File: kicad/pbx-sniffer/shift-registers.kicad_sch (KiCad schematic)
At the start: 1 part, among them U2 74LS165

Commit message: more shift register work
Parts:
- added J49: Conn_01x02_Socket, Connector_PinSocket_2.54mm:PinSocket_1x02_P2.54mm_Vertical, symbol Connector:Conn_01x02_Socket
- added R1: 10k, symbol Device:R
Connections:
- net +5V: now also J49.2 (Pin_2)
- net GND: now also R1.2
- net at U2.11 (D0): now also J49.1 (Pin_1), R1.1

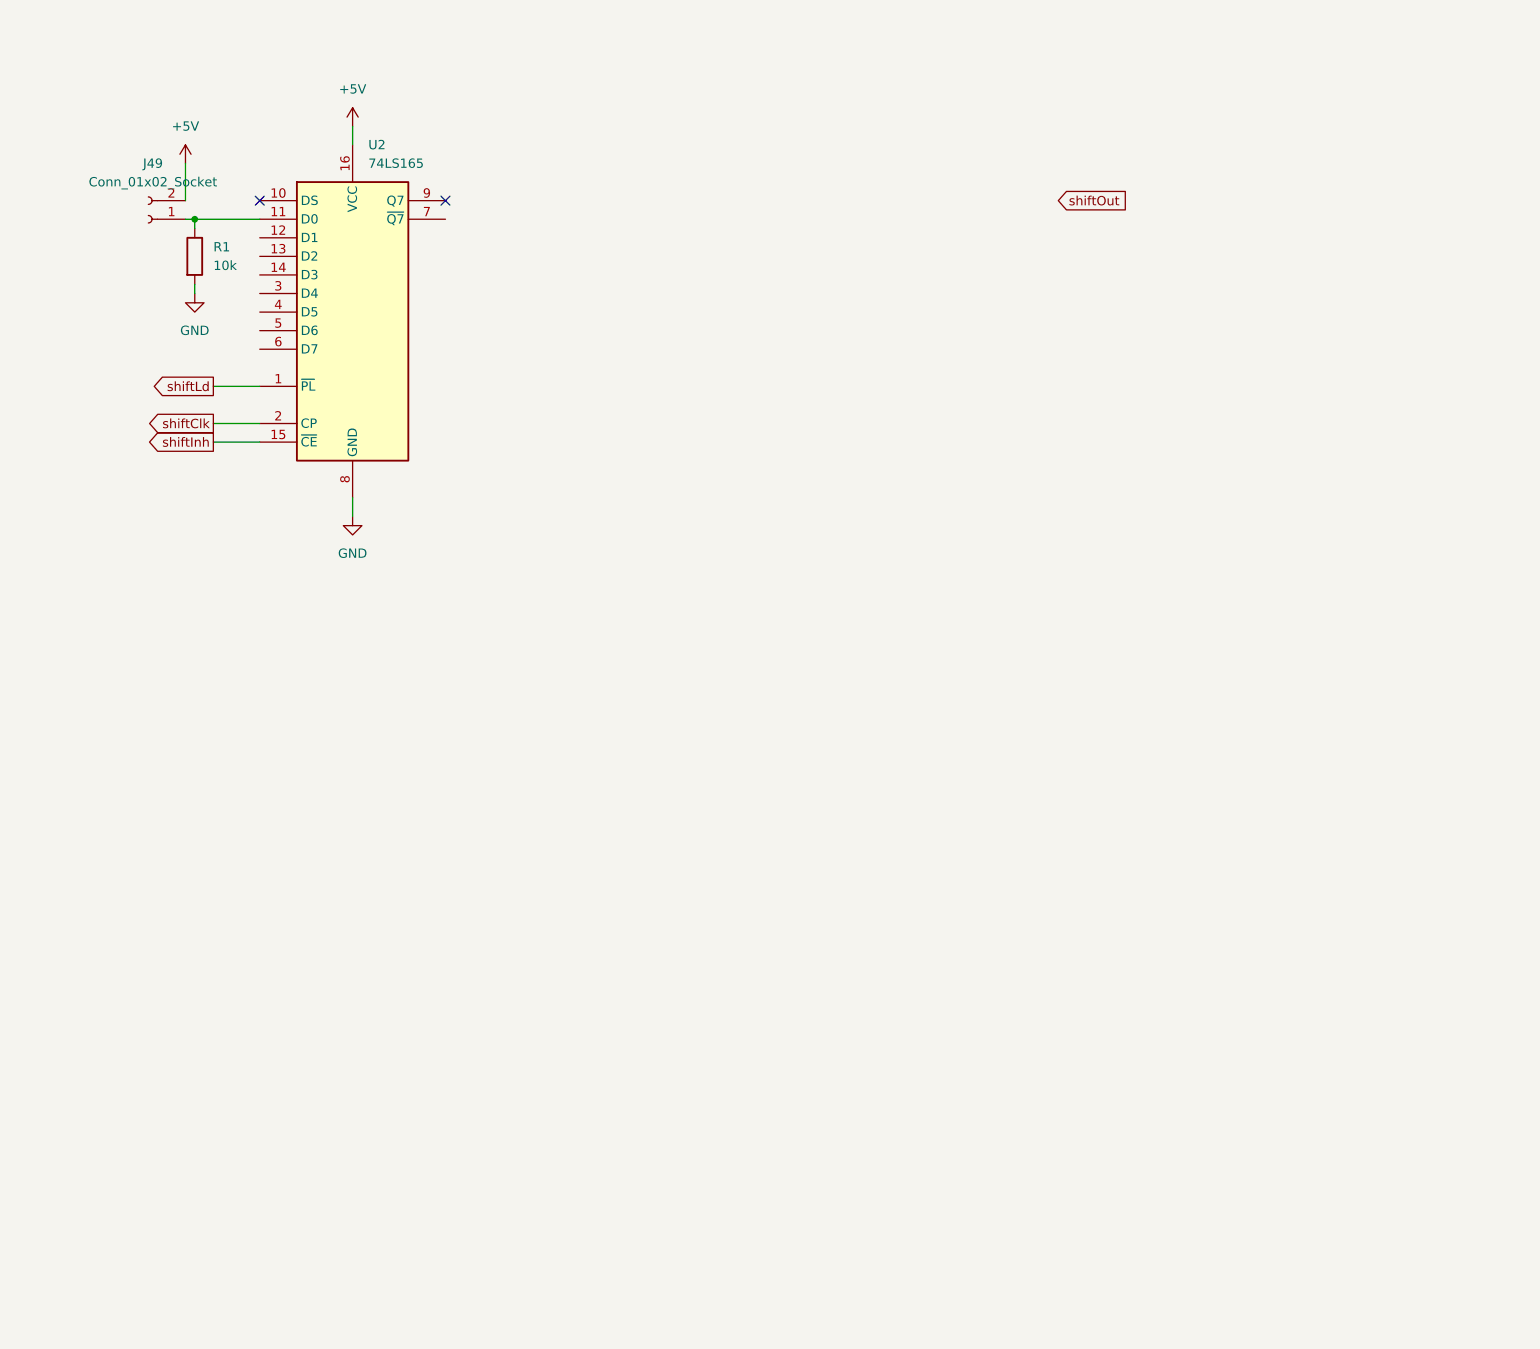
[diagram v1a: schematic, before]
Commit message: shift register page assembled for 16 phones
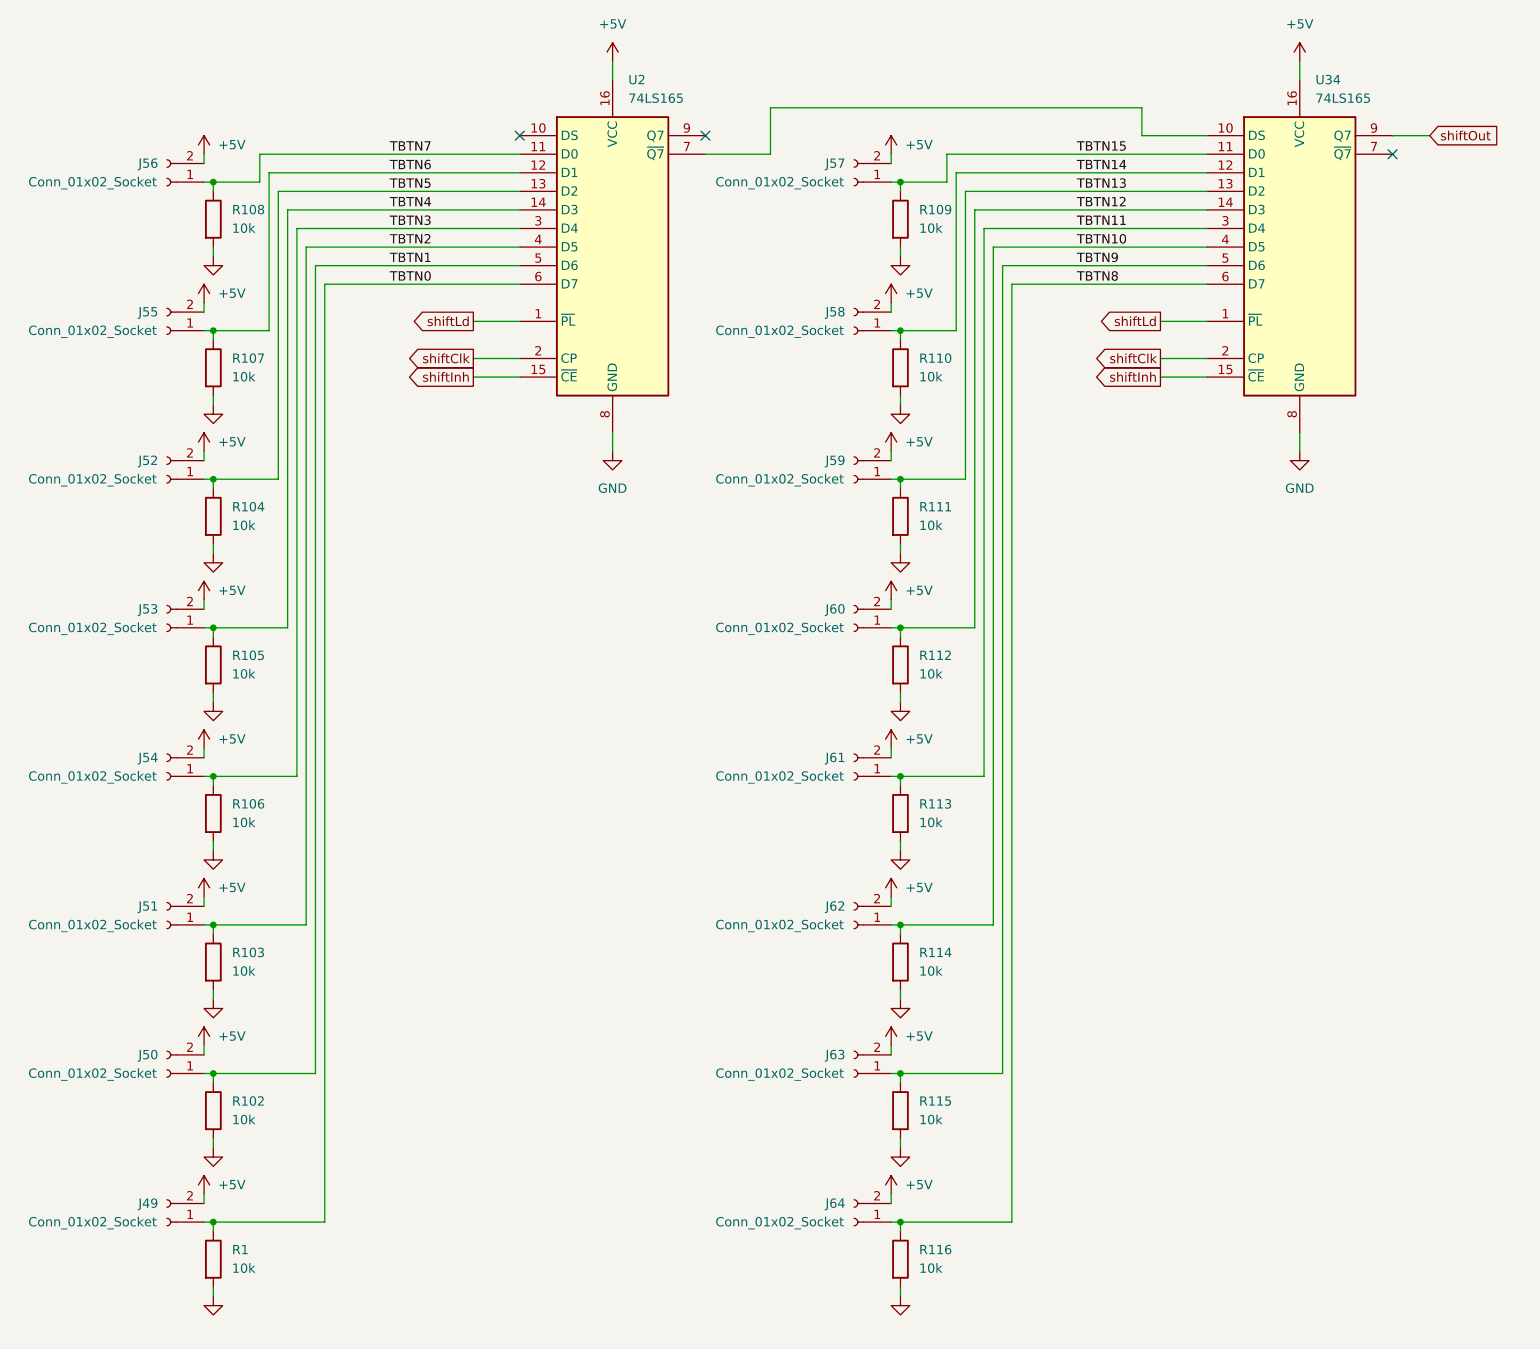
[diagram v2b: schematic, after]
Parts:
- added J50, J51, J52, J53, J54, J55, J56, J57, J58, J59, J60, J61, J62, J63, J64: Conn_01x02_Socket, Connector_PinSocket_2.54mm:PinSocket_1x02_P2.54mm_Vertical, symbol Connector:Conn_01x02_Socket
- added R102, R103, R104, R105, R106, R107, R108, R109, R110, R111, R112, R113, R114, R115, R116: 10k, symbol Device:R
- added U34: 74LS165, symbol 74xx:74LS165
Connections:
- net +5V: now also J50.2 (Pin_2), J51.2 (Pin_2), J52.2 (Pin_2), J53.2 (Pin_2), J54.2 (Pin_2), J55.2 (Pin_2), J56.2 (Pin_2), J57.2 (Pin_2), J58.2 (Pin_2), J59.2 (Pin_2), J60.2 (Pin_2), J61.2 (Pin_2), J62.2 (Pin_2), J63.2 (Pin_2), J64.2 (Pin_2), U34.16 (VCC)
- net GND: now also R102.2, R103.2, R104.2, R105.2, R106.2, R107.2, R108.2, R109.2, R110.2, R111.2, R112.2, R113.2, R114.2, R115.2, R116.2, U34.8 (GND)
- net shiftClk: now also U34.2 (CP)
- net shiftInh: now also U34.15 (~{CE})
- net shiftLd: now also U34.1 (~{PL})
- net shiftOut: now also U34.9 (Q7)
- net TBTN0: now reaches J49.1 (Pin_1), R1.1
- net TBTN0: now also U2.6 (D7); no longer U2.11 (D0)
- net TBTN6: now reaches U2.12 (D1)
- net TBTN6: now also J55.1 (Pin_1), R107.1
- net TBTN5: now reaches U2.13 (D2)
- net TBTN5: now also J52.1 (Pin_1), R104.1
- net TBTN4: now reaches U2.14 (D3)
- net TBTN4: now also J53.1 (Pin_1), R105.1
- net TBTN3: now reaches U2.3 (D4)
- net TBTN3: now also J54.1 (Pin_1), R106.1
- net TBTN2: now reaches U2.4 (D5)
- net TBTN2: now also J51.1 (Pin_1), R103.1
- net TBTN1: now reaches U2.5 (D6)
- net TBTN1: now also J50.1 (Pin_1), R102.1
- net at U2.7 (~{Q7}): now also U34.10 (DS)
- new net TBTN10: J62.1 (Pin_1), R114.1, U34.4 (D5)
- new net TBTN11: J61.1 (Pin_1), R113.1, U34.3 (D4)
- new net TBTN12: J60.1 (Pin_1), R112.1, U34.14 (D3)
- new net TBTN13: J59.1 (Pin_1), R111.1, U34.13 (D2)
- new net TBTN14: J58.1 (Pin_1), R110.1, U34.12 (D1)
- new net TBTN15: J57.1 (Pin_1), R109.1, U34.11 (D0)
- new net TBTN7: J56.1 (Pin_1), R108.1, U2.11 (D0)
- new net TBTN8: J64.1 (Pin_1), R116.1, U34.6 (D7)
- new net TBTN9: J63.1 (Pin_1), R115.1, U34.5 (D6)
- no-connect marks 2 -> 3
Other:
- moved on the sheet: J49, R1, U2

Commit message: organize jacks in the pcb layout
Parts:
- R1, R102, R103, R104, R105, R106, R107, R108, R109, R110, R111, R112, R113, R114, R115, R116: footprint (none) -> Resistor_THT:R_Axial_DIN0207_L6.3mm_D2.5mm_P10.16mm_Horizontal
- U2, U34: footprint (none) -> Package_DIP:DIP-16_W7.62mm
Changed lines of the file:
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@@
 			)
 		)
-		(property "Footprint" ""
+		(property "Footprint" "Resistor_THT:R_Axial_DIN0207_L6.3mm_D2.5mm_P10.16mm_Horizontal"
 			(at 40.132 165.1 90)
 			(effects
@@
 			)
 		)
-		(property "Footprint" ""
+		(property "Footprint" "Package_DIP:DIP-16_W7.62mm"
 			(at 96.52 46.99 0)
 			(effects
@@
 			)
 		)
-		(property "Footprint" ""
+		(property "Footprint" "Resistor_THT:R_Axial_DIN0207_L6.3mm_D2.5mm_P10.16mm_Horizontal"
 			(at 134.112 63.5 90)
 			(effects
@@
 			)
 		)
-		(property "Footprint" ""
+		(property "Footprint" "Resistor_THT:R_Axial_DIN0207_L6.3mm_D2.5mm_P10.16mm_Horizontal"
 			(at 134.112 124.46 90)
 			(effects
@@
 			)
 		)
-		(property "Footprint" ""
+		(property "Footprint" "Resistor_THT:R_Axial_DIN0207_L6.3mm_D2.5mm_P10.16mm_Horizontal"
 			(at 40.132 185.42 90)
 			(effects
@@
 			)
 		)
-		(property "Footprint" ""
+		(property "Footprint" "Resistor_THT:R_Axial_DIN0207_L6.3mm_D2.5mm_P10.16mm_Horizontal"
 			(at 134.112 185.42 90)
 			(effects
@@
 			)
 		)
-		(property "Footprint" ""
+		(property "Footprint" "Resistor_THT:R_Axial_DIN0207_L6.3mm_D2.5mm_P10.16mm_Horizontal"
 			(at 134.112 104.14 90)
 			(effects
@@
 			)
 		)
-		(property "Footprint" ""
+		(property "Footprint" "Resistor_THT:R_Axial_DIN0207_L6.3mm_D2.5mm_P10.16mm_Horizontal"
 			(at 134.112 165.1 90)
 			(effects
@@
 			)
 		)
-		(property "Footprint" ""
+		(property "Footprint" "Package_DIP:DIP-16_W7.62mm"
 			(at 190.5 46.99 0)
 			(effects
@@
 			)
 		)
-		(property "Footprint" ""
+		(property "Footprint" "Resistor_THT:R_Axial_DIN0207_L6.3mm_D2.5mm_P10.16mm_Horizontal"
 			(at 40.132 43.18 90)
 			(effects
@@
 			)
 		)
-		(property "Footprint" ""
+		(property "Footprint" "Resistor_THT:R_Axial_DIN0207_L6.3mm_D2.5mm_P10.16mm_Horizontal"
 			(at 40.132 104.14 90)
 			(effects
@@
 			)
 		)
-		(property "Footprint" ""
+		(property "Footprint" "Resistor_THT:R_Axial_DIN0207_L6.3mm_D2.5mm_P10.16mm_Horizontal"
 			(at 134.112 144.78 90)
 			(effects
@@
 			)
 		)
-		(property "Footprint" ""
+		(property "Footprint" "Resistor_THT:R_Axial_DIN0207_L6.3mm_D2.5mm_P10.16mm_Horizontal"
 			(at 134.112 43.18 90)
 			(effects
@@
 			)
 		)
-		(property "Footprint" ""
+		(property "Footprint" "Resistor_THT:R_Axial_DIN0207_L6.3mm_D2.5mm_P10.16mm_Horizontal"
 			(at 40.132 144.78 90)
 			(effects
@@
 			)
 		)
-		(property "Footprint" ""
+		(property "Footprint" "Resistor_THT:R_Axial_DIN0207_L6.3mm_D2.5mm_P10.16mm_Horizontal"
 			(at 134.112 83.82 90)
 			(effects
@@
 			)
 		)
-		(property "Footprint" ""
+		(property "Footprint" "Resistor_THT:R_Axial_DIN0207_L6.3mm_D2.5mm_P10.16mm_Horizontal"
 			(at 40.132 124.46 90)
 			(effects
@@
 			)
 		)
-		(property "Footprint" ""
+		(property "Footprint" "Resistor_THT:R_Axial_DIN0207_L6.3mm_D2.5mm_P10.16mm_Horizontal"
 			(at 40.132 83.82 90)
 			(effects
@@
 			)
 		)
-		(property "Footprint" ""
+		(property "Footprint" "Resistor_THT:R_Axial_DIN0207_L6.3mm_D2.5mm_P10.16mm_Horizontal"
 			(at 40.132 63.5 90)
 			(effects

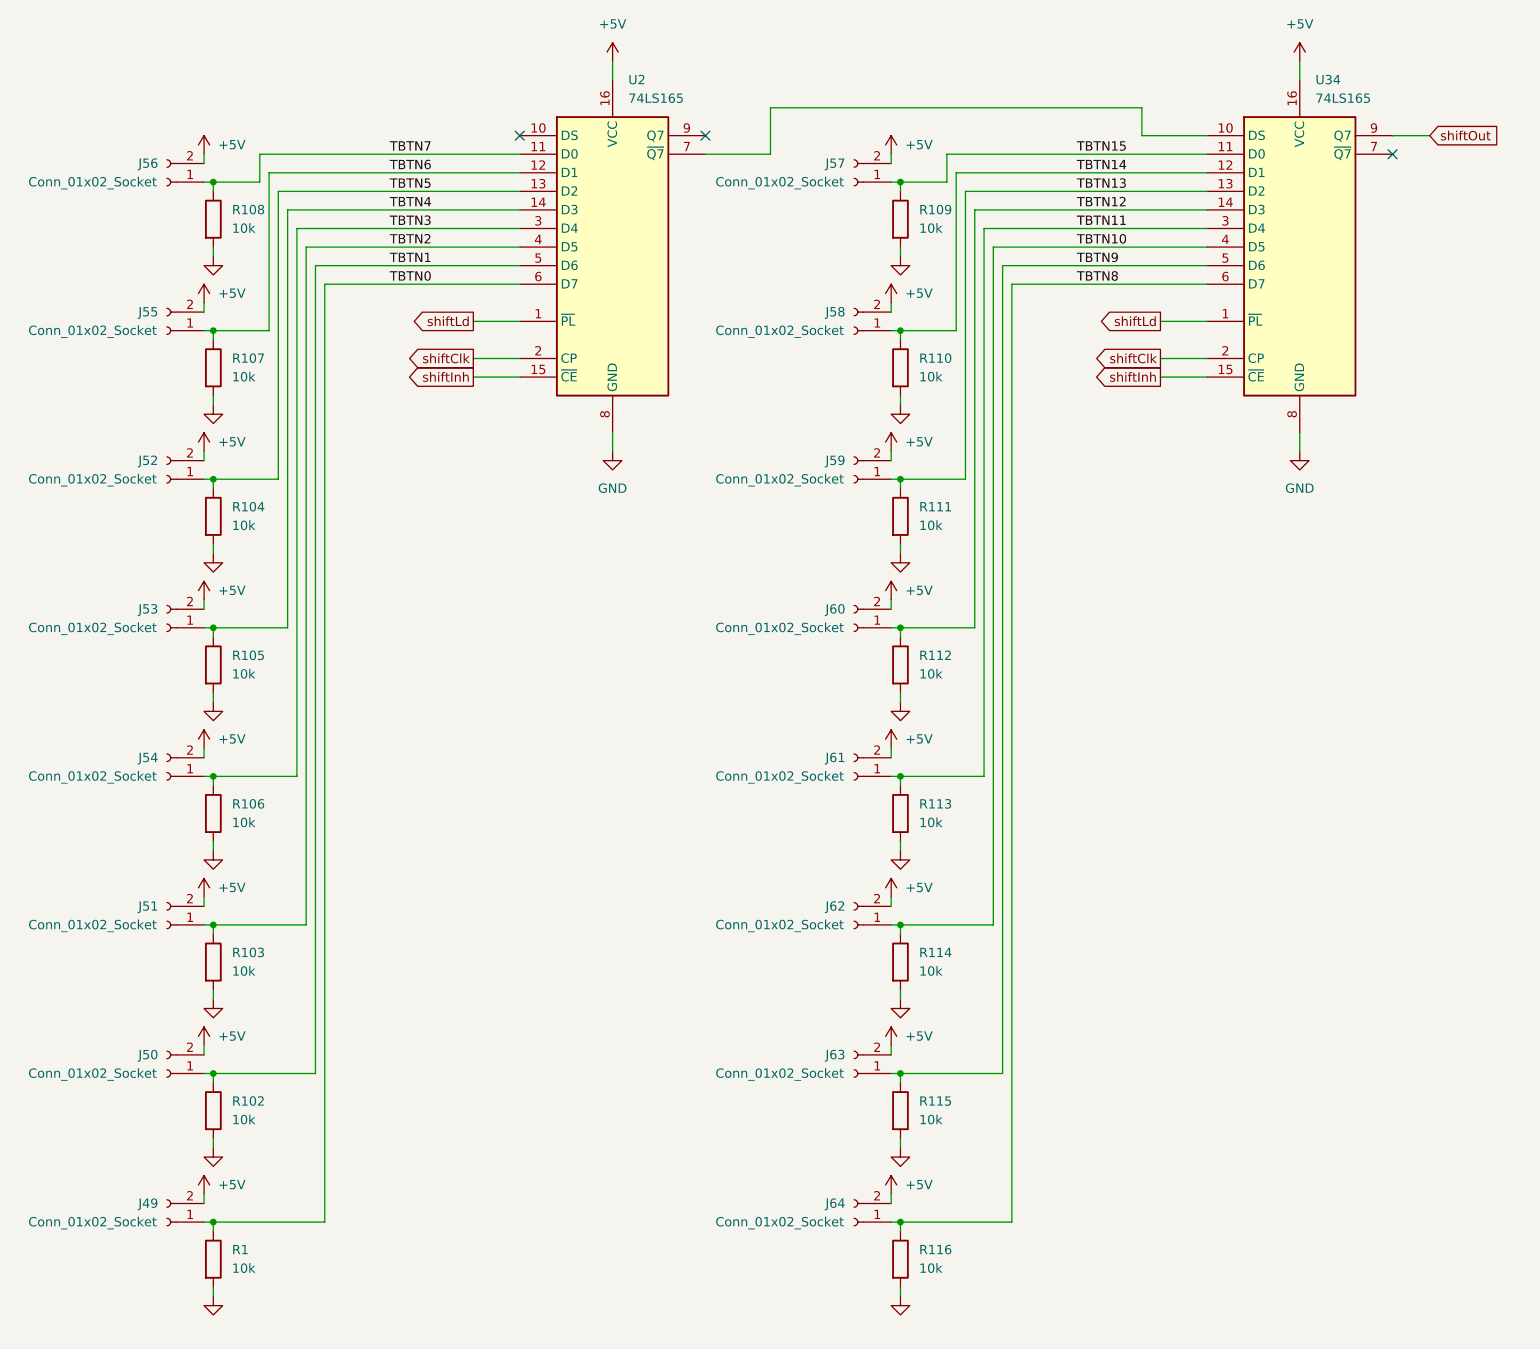
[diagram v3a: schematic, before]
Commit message: redid wiring in order to make power planes doable
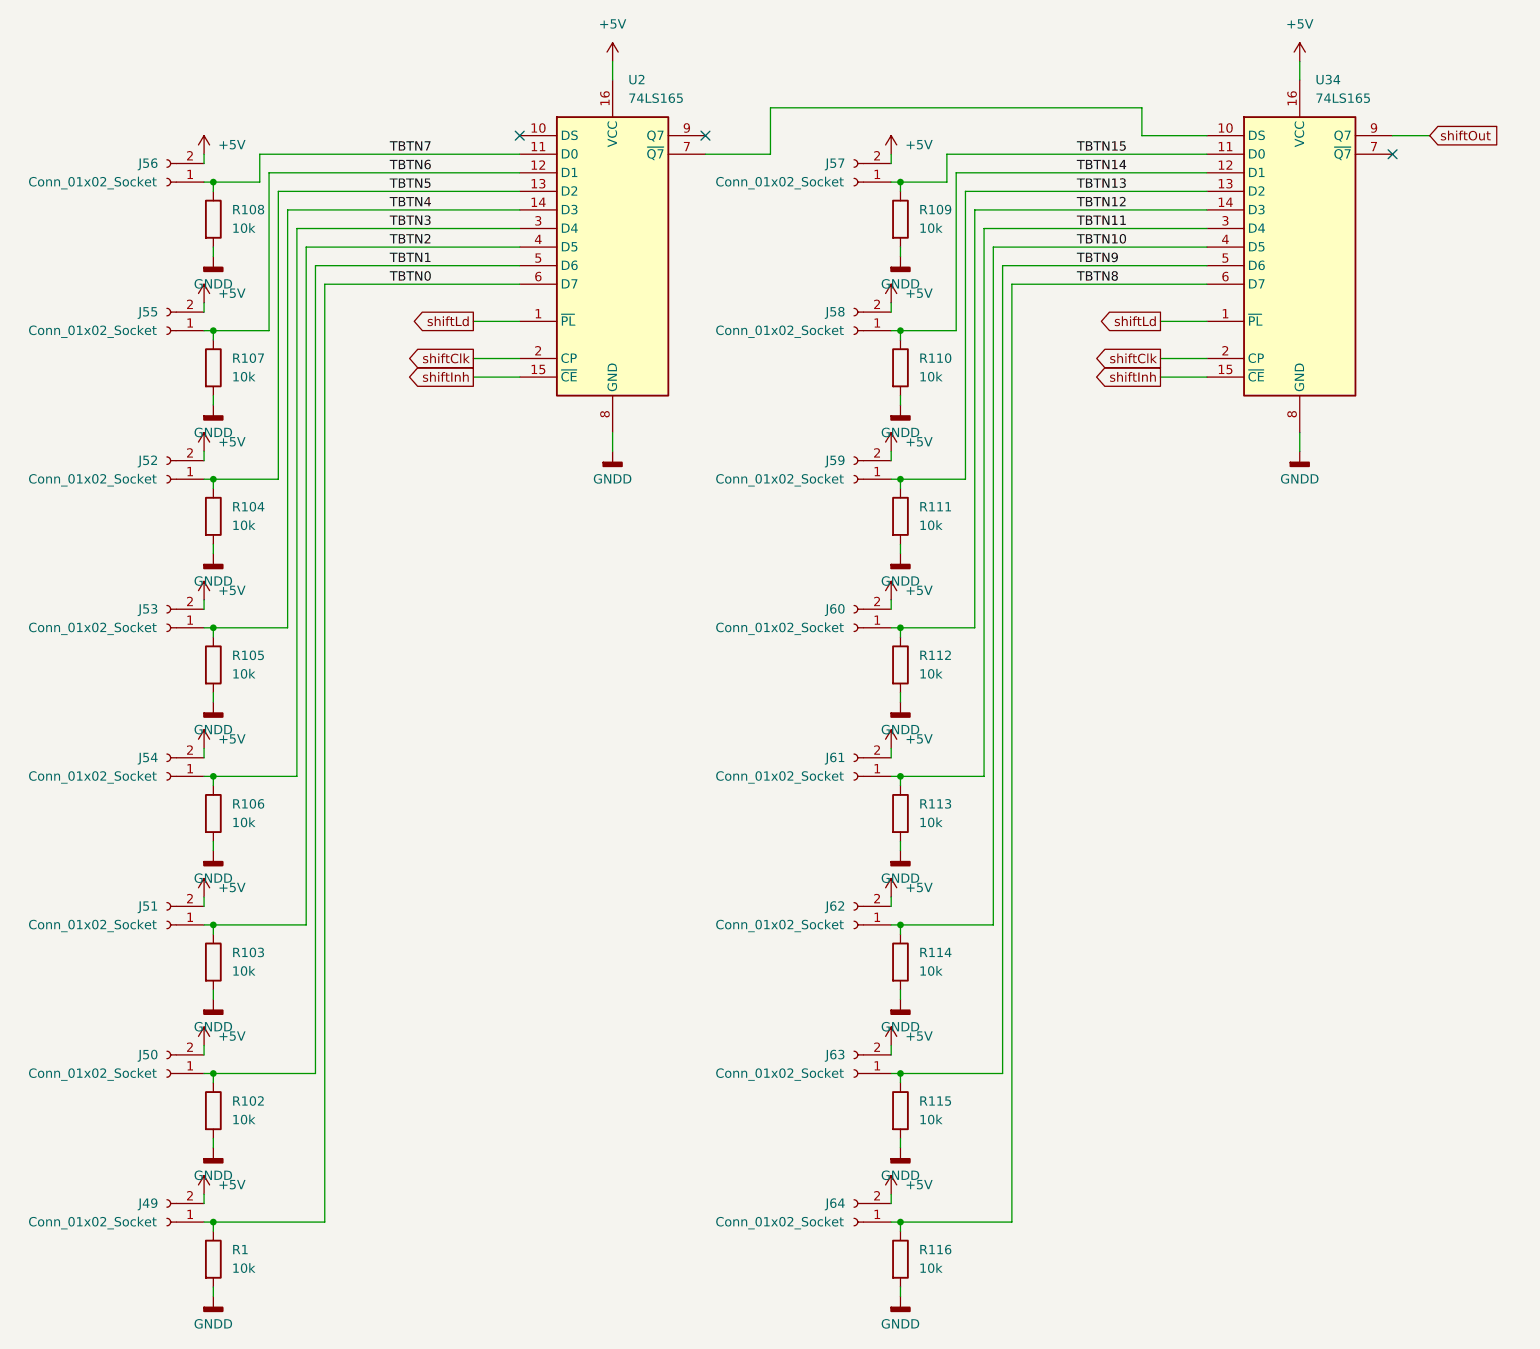
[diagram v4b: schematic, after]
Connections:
- net GND renamed GNDD
